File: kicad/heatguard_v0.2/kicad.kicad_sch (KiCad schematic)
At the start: 31 parts, among them J11 Conn_01x12, J12 Conn_01x12, J13 Conn_01x12, J14 Conn_01x12, J2 Conn_01x12, J20 Conn_01x01, J3 Conn_01x12, J4 Conn_01x12, J5 Conn_01x12, J6 Conn_01x12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

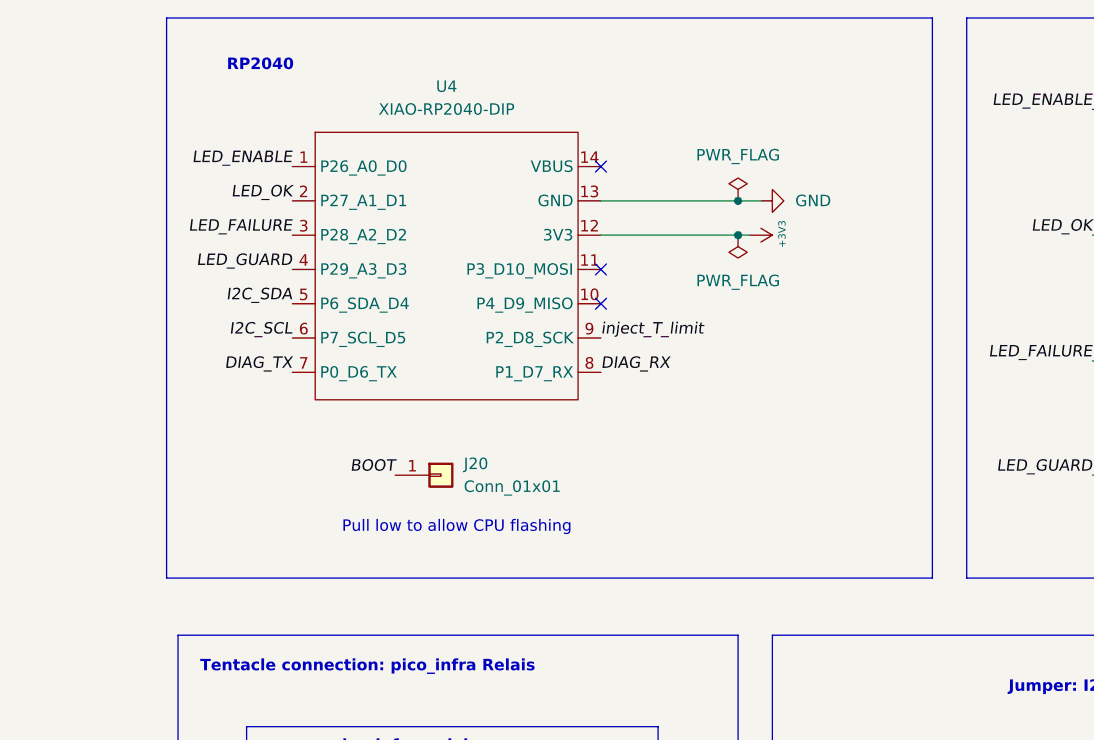
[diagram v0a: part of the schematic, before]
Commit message: v0.2: XIAO: Now smd (was on pins)
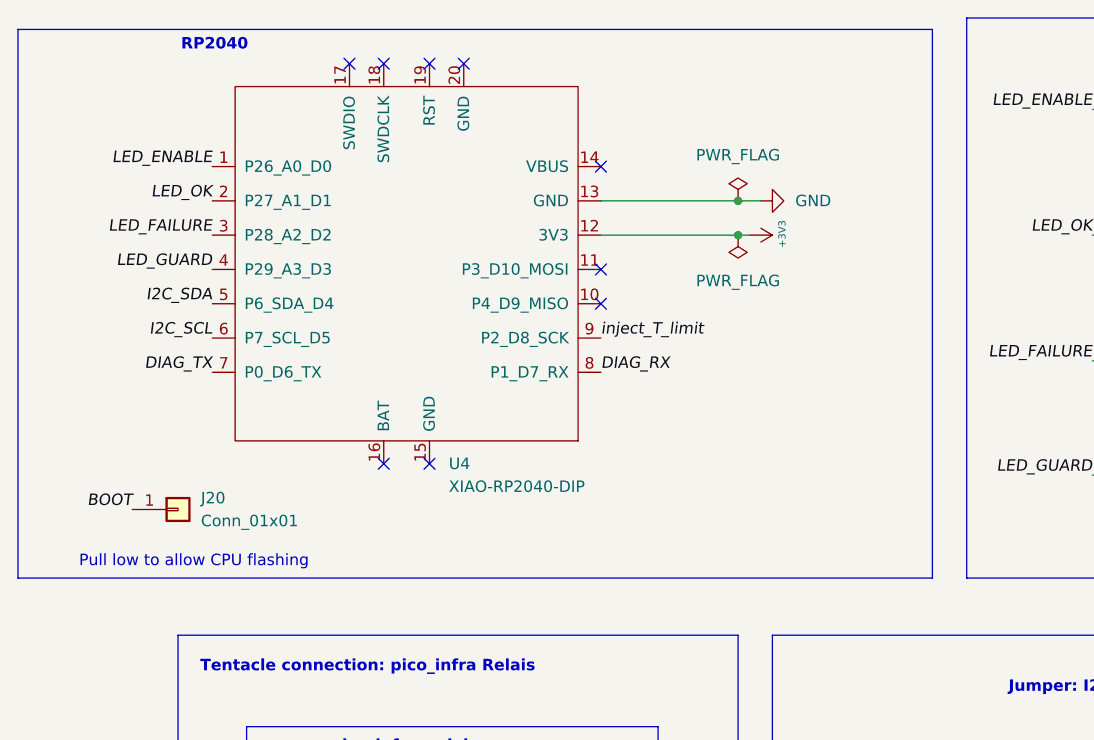
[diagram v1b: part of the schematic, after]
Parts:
- U4: footprint 00_project_library:XIAO-RP2040-DIP -> 00_project_library:XIAO-RP2040-SMD; symbol 00_project_library:XIAO-RP2040-DIP -> 00_project_library:XIAO-RP2040-SMD; now in the parts list
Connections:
- no-connect marks 7 -> 13
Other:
- moved on the sheet: J20
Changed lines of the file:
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@@
 	)
 	(rectangle
-		(start 146.05 33.02)
+		(start 129.54 34.29)
 		(end 231.14 95.25)
 		(stroke
@@
 	(text "Pull low to allow CPU flashing"
 		(exclude_from_sim no)
-		(at 178.308 89.662 0)
+		(at 149.098 93.472 0)
 		(effects
 			(font
@@
 	(text "RP2040"
 		(exclude_from_sim no)
-		(at 156.464 38.354 0)
+		(at 151.384 36.068 0)
 		(effects
 			(font
@@
 	)
 	(no_connect
+		(at 170.18 38.1)
+	)
+	(no_connect
 		(at 298.45 54.61)
 	)
 	(no_connect
+		(at 175.26 82.55)
+	)
+	(no_connect
 		(at 298.45 43.18)
 	)
 	(no_connect
+		(at 179.07 38.1)
+	)
+	(no_connect
+		(at 170.18 82.55)
+	)
+	(no_connect
+		(at 166.37 38.1)
+	)
+	(no_connect
 		(at 194.31 49.53)
 	)
@@
 		(at 298.45 50.8)
 	)
+	(no_connect
+		(at 175.26 38.1)
+	)
 	(wire
 		(pts
@@
 	)
 	(label "DIAG_TX"
-		(at 160.02 72.39 180)
+		(at 151.13 72.39 180)
 		(effects
 			(font
@@
 	)
 	(label "LED_FAILURE"
-		(at 160.02 57.15 180)
+		(at 151.13 57.15 180)
 		(effects
 			(font
@@
 	)
 	(label "I2C_SDA"
-		(at 160.02 64.77 180)
+		(at 151.13 64.77 180)
 		(effects
 			(font
@@
 	)
 	(label "LED_OK"
-		(at 160.02 53.34 180)
+		(at 151.13 53.34 180)
 		(effects
 			(font
@@
 	)
 	(label "LED_ENABLE"
-		(at 160.02 49.53 180)
+		(at 151.13 49.53 180)
 		(effects
 			(font
@@
 	)
 	(label "LED_GUARD"
-		(at 160.02 60.96 180)
+		(at 151.13 60.96 180)
 		(effects
 			(font
@@
 	)
 	(label "BOOT"
-		(at 171.45 83.82 180)
+		(at 142.24 87.63 180)
 		(effects
 			(font
@@
 	)
 	(label "I2C_SCL"
-		(at 160.02 68.58 180)
+		(at 151.13 68.58 180)
 		(effects
 			(font
@@
 	)
 	(symbol
-		(lib_id "00_project_library:XIAO-RP2040-DIP")
-		(at 175.26 40.64 0)
+		(lib_id "00_project_library:XIAO-RP2040-SMD")
+		(at 172.72 60.96 0)
 		(unit 1)
 		(exclude_from_sim no)
-		(in_bom no)
+		(in_bom yes)
 		(on_board yes)
 		(dnp no)
 		(fields_autoplaced yes)
 		(property "Reference" "U4"
-			(at 177.165 40.64 0)
+			(at 177.4033 82.55 0)
 			(effects
 				(font
 					(size 1.27 1.27)
 				)
+				(justify left)
 			)
 		)
 		(property "Value" "XIAO-RP2040-DIP"
-			(at 177.165 43.18 0)
+			(at 177.4033 85.09 0)
 			(effects
 				(font
 					(size 1.27 1.27)
 				)
+				(justify left)
 			)
 		)
-		(property "Footprint" "00_project_library:XIAO-RP2040-DIP"
-			(at 179.324 77.978 0)
+		(property "Footprint" "00_project_library:XIAO-RP2040-SMD"
+			(at 163.83 55.88 0)
 			(effects
 				(font
@@
 		)
 		(property "Datasheet" ""
-			(at 175.26 40.64 0)
+			(at 163.83 55.88 0)
 			(effects
 				(font
@@
 		)
 		(property "Description" ""
-			(at 175.26 40.64 0)
+			(at 172.72 60.96 0)
 			(effects
 				(font
@@
 		(pin "13"
 		)
+		(pin "18"
+		)
+		(pin "15"
+		)
+		(pin "19"
+		)
+		(pin "17"
+		)
+		(pin "16"
+		)
+		(pin "20"
+		)
 		(instances
 			(project ""
@@
 	(symbol
 		(lib_id "Connector_Generic:Conn_01x01")
-		(at 176.53 83.82 0)
+		(at 147.32 87.63 0)
 		(unit 1)
 		(exclude_from_sim no)
@@
 		(fields_autoplaced yes)
 		(property "Reference" "J20"
-			(at 179.07 82.5499 0)
+			(at 149.86 86.3599 0)
 			(effects
 				(font
@@
 		)
 		(property "Value" "Conn_01x01"
-			(at 179.07 85.0899 0)
+			(at 149.86 88.8999 0)
 			(effects
 				(font
@@
 		)
 		(property "Footprint" "00_project_library:octoprobe_breakout_PB"
-			(at 176.53 83.82 0)
+			(at 147.32 87.63 0)
 			(effects
 				(font
@@
 		)
 		(property "Datasheet" "~"
-			(at 176.53 83.82 0)
+			(at 147.32 87.63 0)
 			(effects
 				(font
@@
 		)
 		(property "Description" "Generic connector, single row, 01x01, script generated (kicad-library-utils/schlib/autogen/connector/)"
-			(at 176.53 83.82 0)
+			(at 147.32 87.63 0)
 			(effects
 				(font

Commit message: v0.2 ready for review
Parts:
- removed J11, J12, J13, J14: Conn_01x12, 00_project_library:octoprobe_breakout_PB_NC, symbol Connector_Generic:Conn_01x01
- removed J2, J3, J4, J5, J6: Conn_01x12, 00_project_library:PinSocket_1x2_P2.54mm_Vertical_squarepad, symbol Connector_Generic:Conn_01x02
- added D10, D11, D12: LED WHITE, LED_SMD:LED_0805_2012Metric, symbol 00_project_library:LED WHITE
- added J1: Conn_02x02_Odd_Even, 00_project_library:PinHeader_2x02_P2.54mm_Vertical_back, symbol Connector_Generic:Conn_02x02_Odd_Even
- added J8, J9: Conn_02x04_Odd_Even, 00_project_library:PinHeader_2x04_P2.54mm_Vertical_back, symbol Connector_Generic:Conn_02x04_Odd_Even
- added R11, R12, R13: 2k2, Resistor_SMD:R_0805_2012Metric_Pad1.20x1.40mm_HandSolder, symbol 00_project_library:R
- U4: now left out of the parts list
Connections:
- net BOOT: now also J1.2 (Pin_2)
- net DIAG_RX: now also J8.5 (Pin_5)
- net DIAG_TX: now also J8.7 (Pin_7)
- net GND: now also J1.1 (Pin_1), J1.3 (Pin_3), R11.1, R12.1, R13.1
- net I2C_SCL: now also J8.8 (Pin_8)
- net I2C_SDA: now also J8.6 (Pin_6)
- net inject_T_limit: now also J8.3 (Pin_3)
- net inject_eeprom_disconnect: now also D12.2 (A), J8.4 (Pin_4)
- net inject_tguard_disconnect: now also D11.2 (A), J8.1 (Pin_1)
- net inject_tref_disconnect: now also D10.2 (A), J8.2 (Pin_2)
- new net: D10.1 (K), R11.2
- new net: D12.1 (K), R13.2
- new net: D11.1 (K), R12.2
- no-connect marks 13 -> 18
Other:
- note removed: "Mounting Pads"

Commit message: v0.2 beta
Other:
- note added: "Address: 0x48 0x4C (disconnect)"
- note added: "Address: 0x49 0x4D (disconnect)"
- note added: "Address: 0x50 0x54 (disconnect)"
- note removed: "Address: 0x48 0x4C (simulation)"
- note removed: "Address: 0x49 0x4D (simulation)"
- note removed: "Address: 0x50 0x54 (simulation)"
- moved on the sheet: D1, D2, D3, D4, J20, J8, J9, R1, R2, R3, R4, TH1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

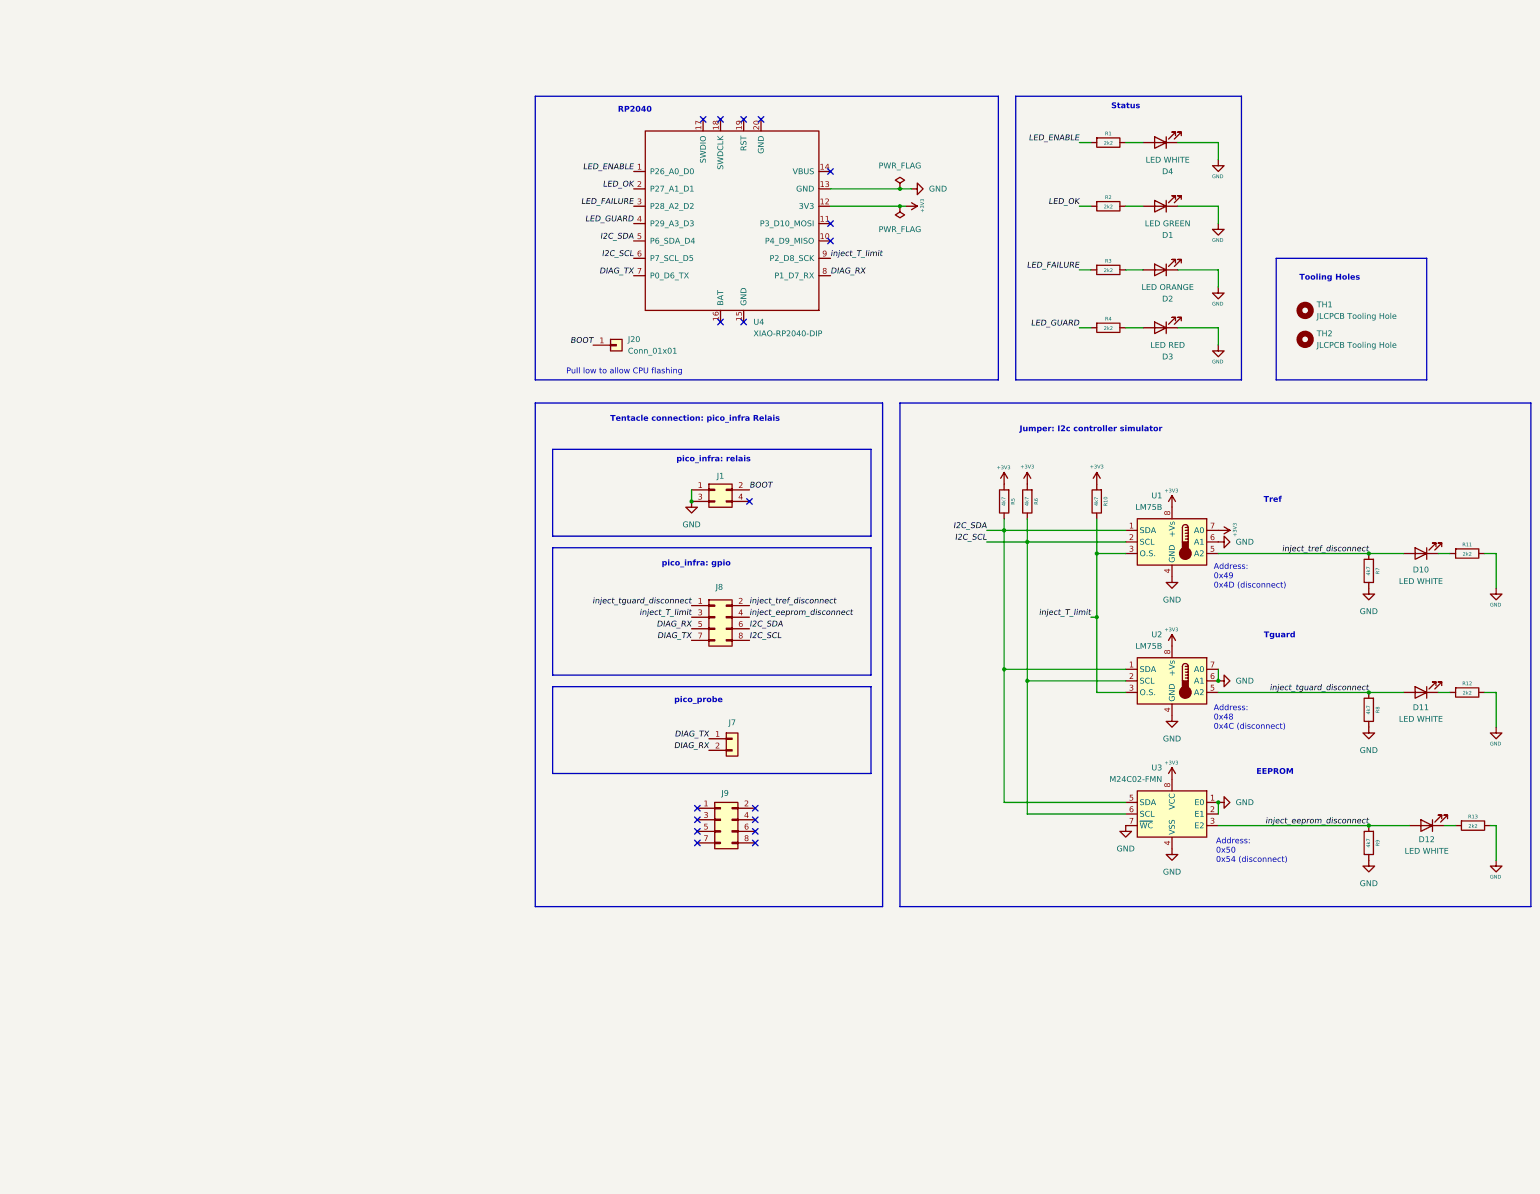
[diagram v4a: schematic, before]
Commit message: Kicad Schematics A3 -> A4
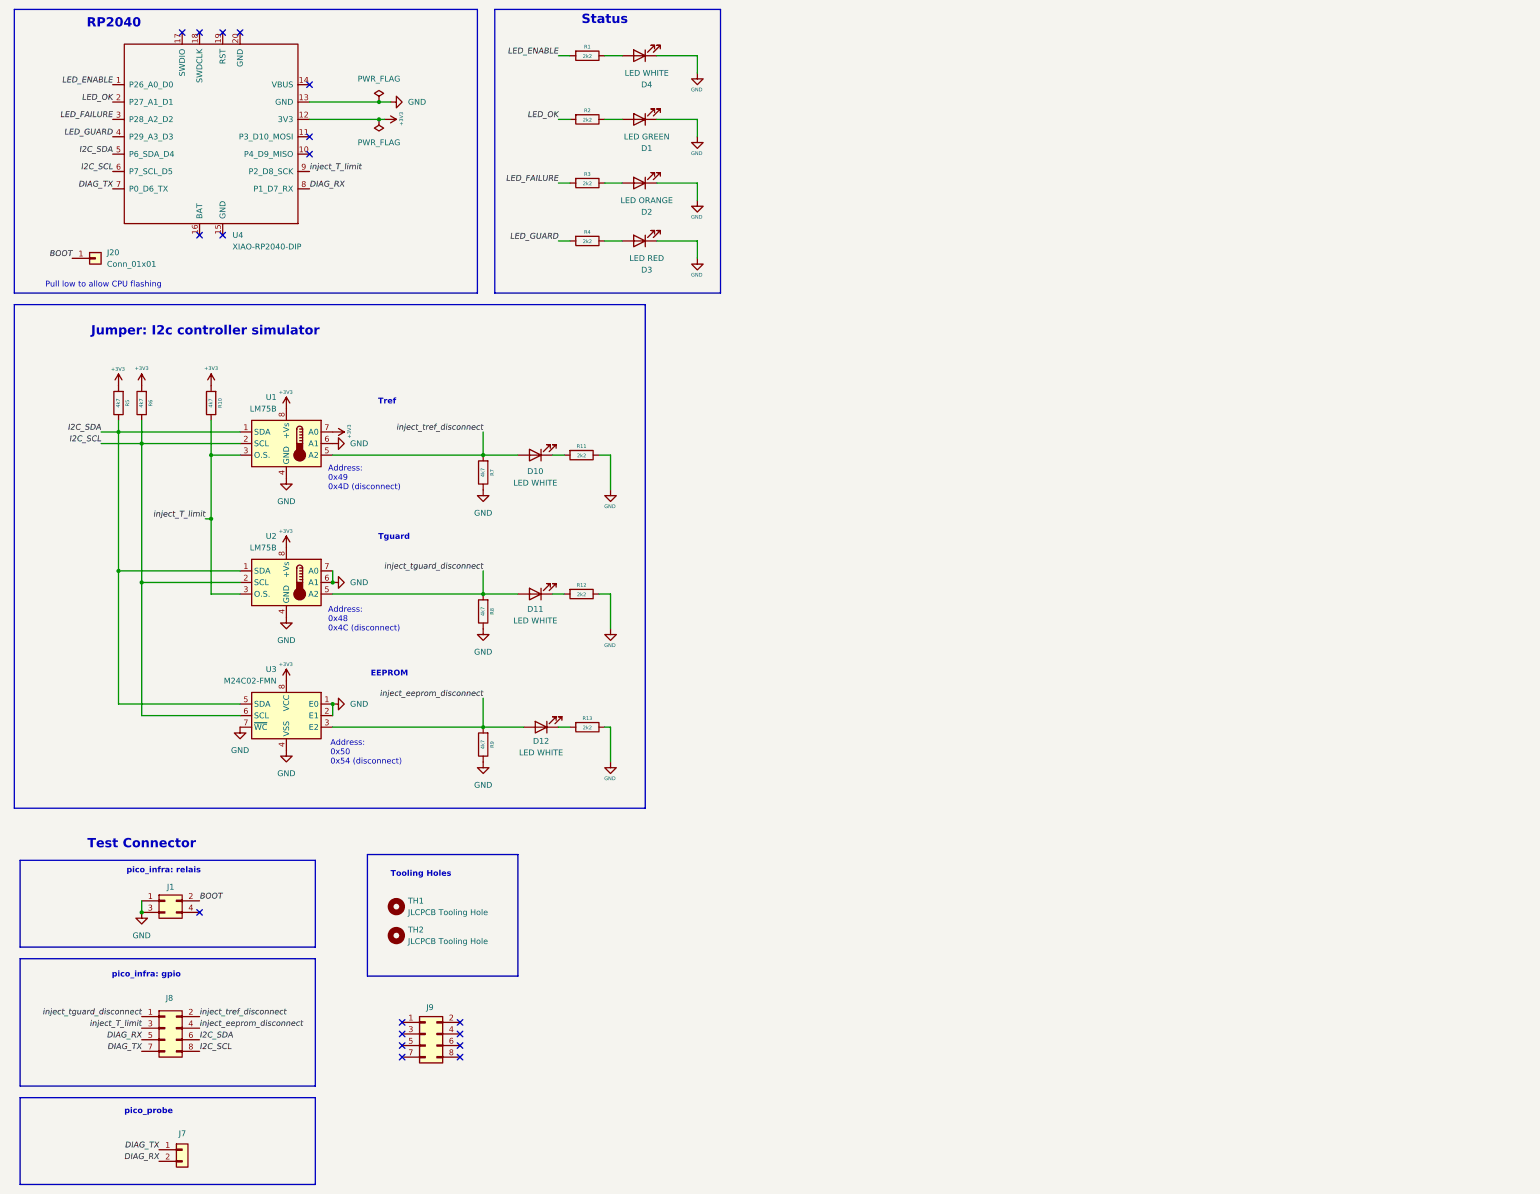
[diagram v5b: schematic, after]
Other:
- note added: "Test Connector"
- note removed: "Tentacle connection: pico_infra Relais"
- moved on the sheet: D1, D10, D11, D12, D2, D3, D4, J1, J20, J7, J8, J9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

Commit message: Use uart of PICO_PROBE
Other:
- note added: "GPIO_PROBE_4 (uart tx)"
- note added: "GPIO_PROBE_5 (uart rx)"
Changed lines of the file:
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@@
+		)
+	)
+	(text "GPIO_PROBE_4 (uart tx)"
+		(exclude_from_sim no)
+		(at 71.12 267.97 0)
+		(effects
+			(font
+				(size 1.27 1.27)
+			)
 		)
 	)
@@
 			)
 		)
+	)
+	(text "GPIO_PROBE_5 (uart rx)"
+		(exclude_from_sim no)
+		(at 71.12 265.43 0)
+		(effects
+			(font
+				(size 1.27 1.27)
+			)
+		)
